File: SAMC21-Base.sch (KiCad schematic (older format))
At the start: 52 parts, among them J1 Conn_01x04, J2 Conn_01x10, J3 Conn_01x10, J5 Conn_ARM_JTAG_SWD_10, U1 ATSAMC21E18A-AUT, U2 TJA1043T, U3 TPS560430Y, U4 MCP1703A, Y1 ABM3-8.000MHZ-D2Y-T

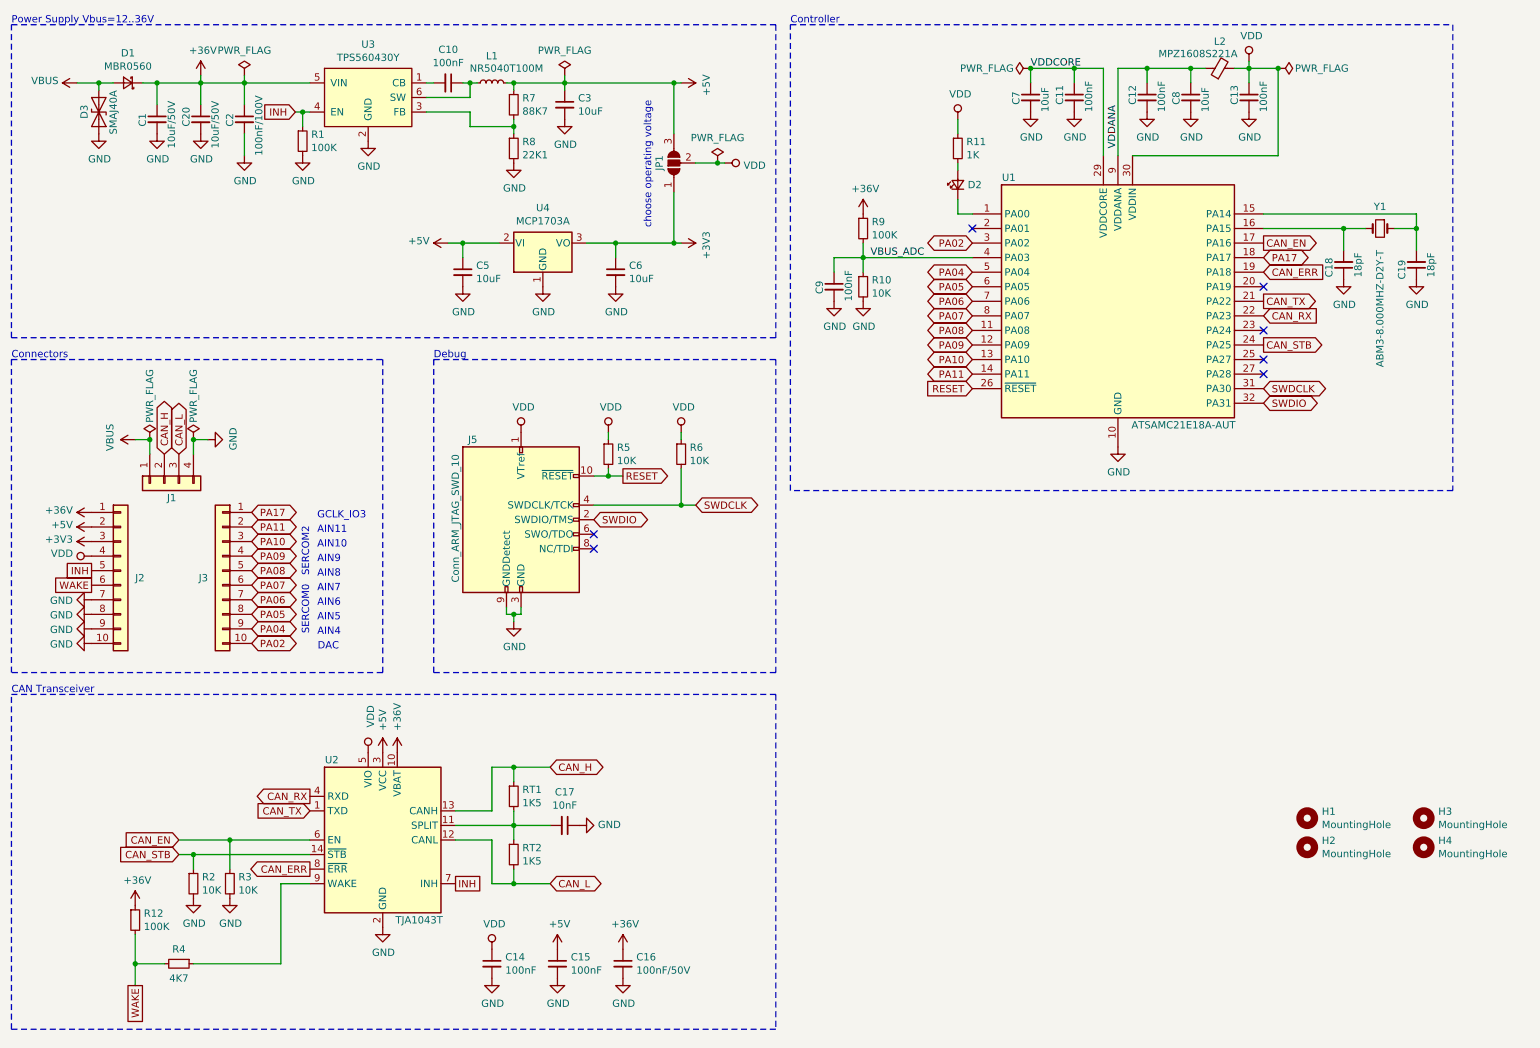
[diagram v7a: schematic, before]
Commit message: add various ESD, EMV and overcurrent protections
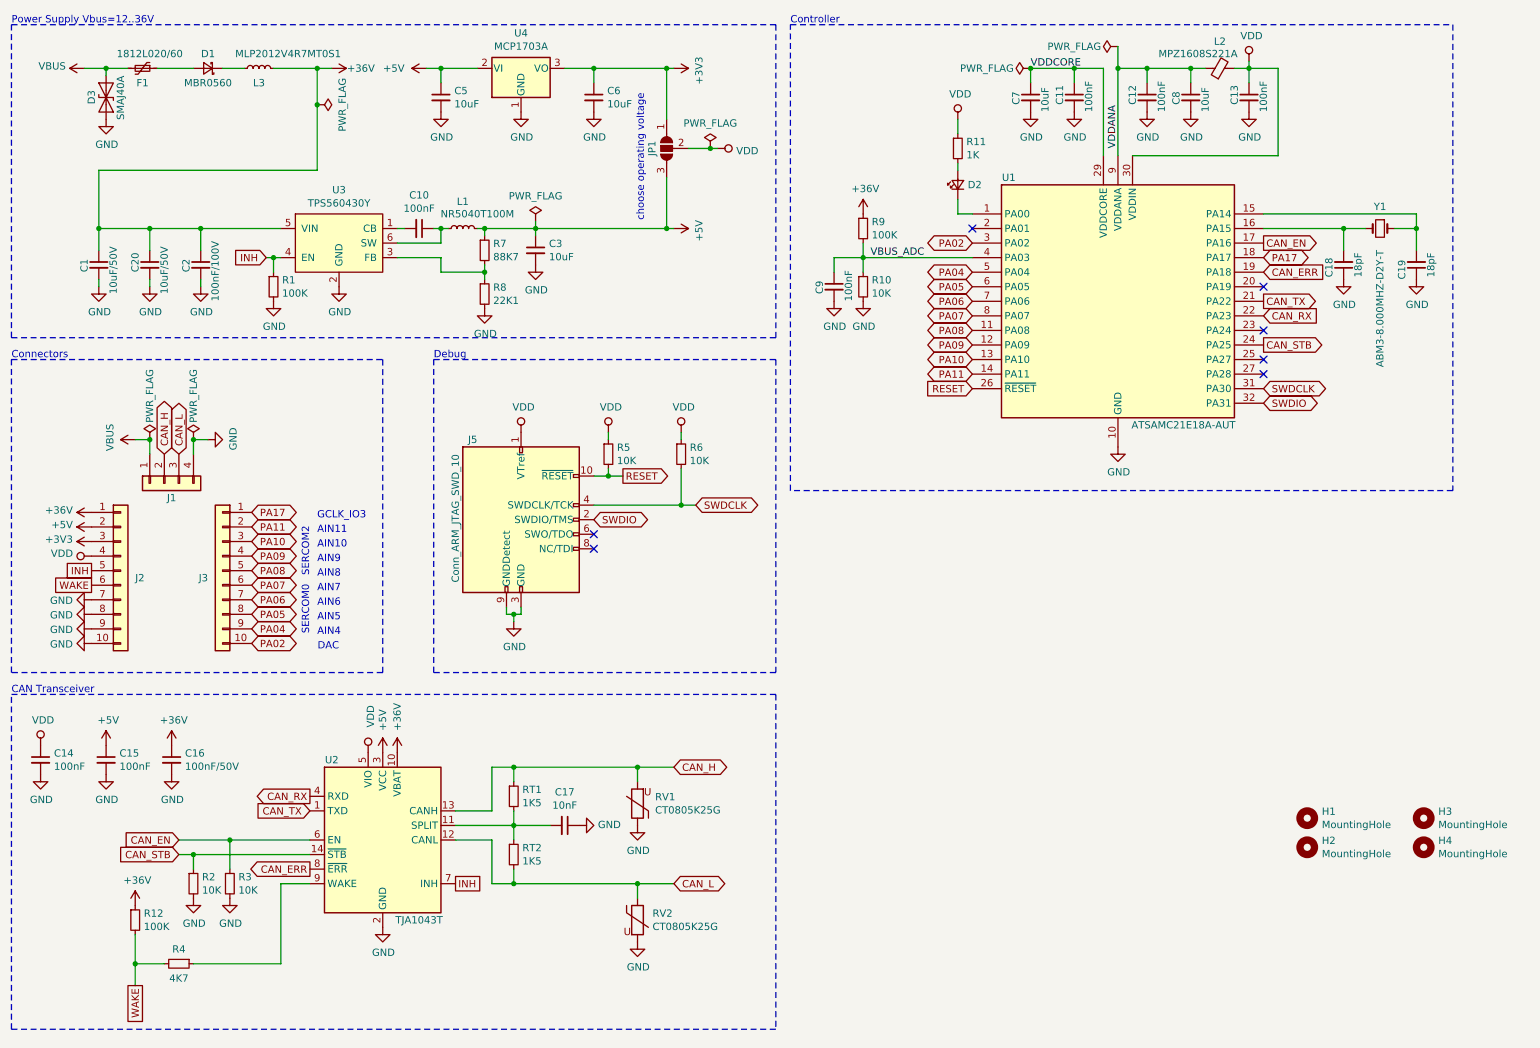
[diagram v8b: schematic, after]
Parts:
- added F1: 1812L020/60, Fuse:Fuse_1812_4532Metric, symbol Device:Polyfuse_Small
- added L3: MLP2012V4R7MT0S1, Inductor_SMD:L_0805_2012Metric, symbol Device:L_Small
- added RV1, RV2: CT0805K25G, Resistor_SMD:R_0805_2012Metric, symbol Device:Varistor
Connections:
- net +36V: now also L3.2; no longer D1.1 (K)
- net CAN_H: now also RV1.2
- net CAN_L: now also RV2.1
- net GND: now also RV1.1, RV2.2
- net VBUS: now also F1.2; no longer D1.2 (A)
- new net: D1.1 (K), L3.1
- new net: D1.2 (A), F1.1
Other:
- moved on the sheet: C1, C10, C14, C15, C16, C2, C20, C3, C5, C6, D1, D3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
